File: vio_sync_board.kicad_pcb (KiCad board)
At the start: 2 copper layers, 53 x 64 mm, 3 parts, among them IC1 Pololu 2595, U1 Pololu D24V5F1

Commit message: layout
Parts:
- A1: footprint Module:RaspberryPi_Pico_Common_Unspecified -> Module:RaspberryPi_Pico_Common_THT
- moved A1 42.9 mm to (50.7, 50.2)
- moved IC1 31.5 mm to (86.6, 78.5), turned to -90 degrees
- moved U1 19.5 mm to (81.2, 66.0)
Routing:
- net Net-(IC1-LV): track 42.5 -> 13.2 mm
- net Net-(A1-GPIO13): track 8.64 -> 35.3 mm
- net Net-(A1-3V3): track 57.3 -> 36.6 mm
- net Net-(U1-GND): track 21.3 -> 18.4 mm
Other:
- board outline removed

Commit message: fix traces, add text
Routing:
- net Net-(A1-3V3): track 36.6 -> 48.4 mm
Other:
- board outline added: 45 x 55 mm
- board text added: "VIO SYNC"
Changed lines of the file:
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@@
+		)
+	)
+	(gr_rect
+		(start 46 47.5)
+		(end 91 102.5)
+		(stroke
+			(width 0.05)
+			(type default)
+		)
+		(fill no)
+		(layer "Edge.Cuts")
+	)
+	(gr_text "VIO SYNC"
+		(at 74.5 97 0)
+		(layer "F.SilkS")
+		(effects
+			(font
+				(size 1.5 1.5)
+				(thickness 0.2)
+				(bold yes)
+			)
+			(justify left bottom)
 		)
 	)
@@
 	)
 	(segment
+		(start 86.58 86.12)
+		(end 83.5 83.04)
+		(width 0.2)
+		(layer "B.Cu")
+		(net 12)
+	)
+	(segment
 		(start 74.32 60.4)
 		(end 68.5 60.4)
@@
 	)
 	(segment
-		(start 86.58 86.12)
-		(end 82.824 82.364)
+		(start 75 68.5)
+		(end 78.5 68.5)
+		(width 0.2)
+		(layer "B.Cu")
+		(net 12)
+	)
+	(segment
+		(start 83.5 83)
+		(end 76 83)
+		(width 0.2)
+		(layer "B.Cu")
+		(net 12)
+	)
+	(segment
+		(start 73.5 80.5)
+		(end 73.5 70)
 		(width 0.2)
 		(layer "B.Cu")
@@
 	)
 	(segment
-		(start 82.824 68.904)
+		(start 79.92 67.08)
 		(end 79.92 66)
 		(width 0.2)
@@
 	)
 	(segment
-		(start 82.824 82.364)
-		(end 82.824 68.904)
+		(start 78.5 68.5)
+		(end 79.92 67.08)
 		(width 0.2)
 		(layer "B.Cu")
+		(net 12)
+	)
+	(segment
+		(start 73.5 70)
+		(end 75 68.5)
+		(width 0.2)
+		(layer "B.Cu")
+		(net 12)
+	)
+	(segment
+		(start 76 83)
+		(end 73.5 80.5)
+		(width 0.2)
+		(layer "B.Cu")
+		(net 12)
+	)
+	(segment
+		(start 83.5 83.04)
+		(end 83.5 83)
+		(width 0.2)
+		(layer "B.Cu")

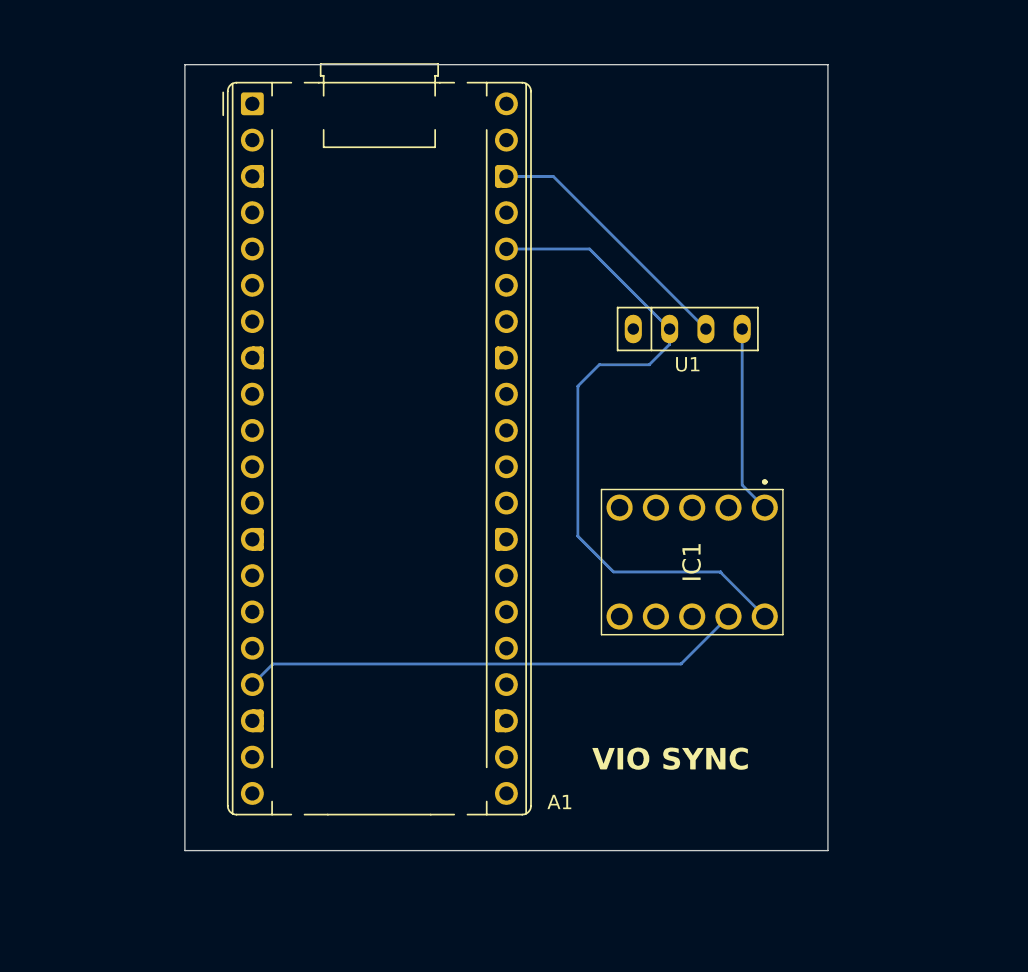
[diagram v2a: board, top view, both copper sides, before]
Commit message: update 1.8v dc convert footprint
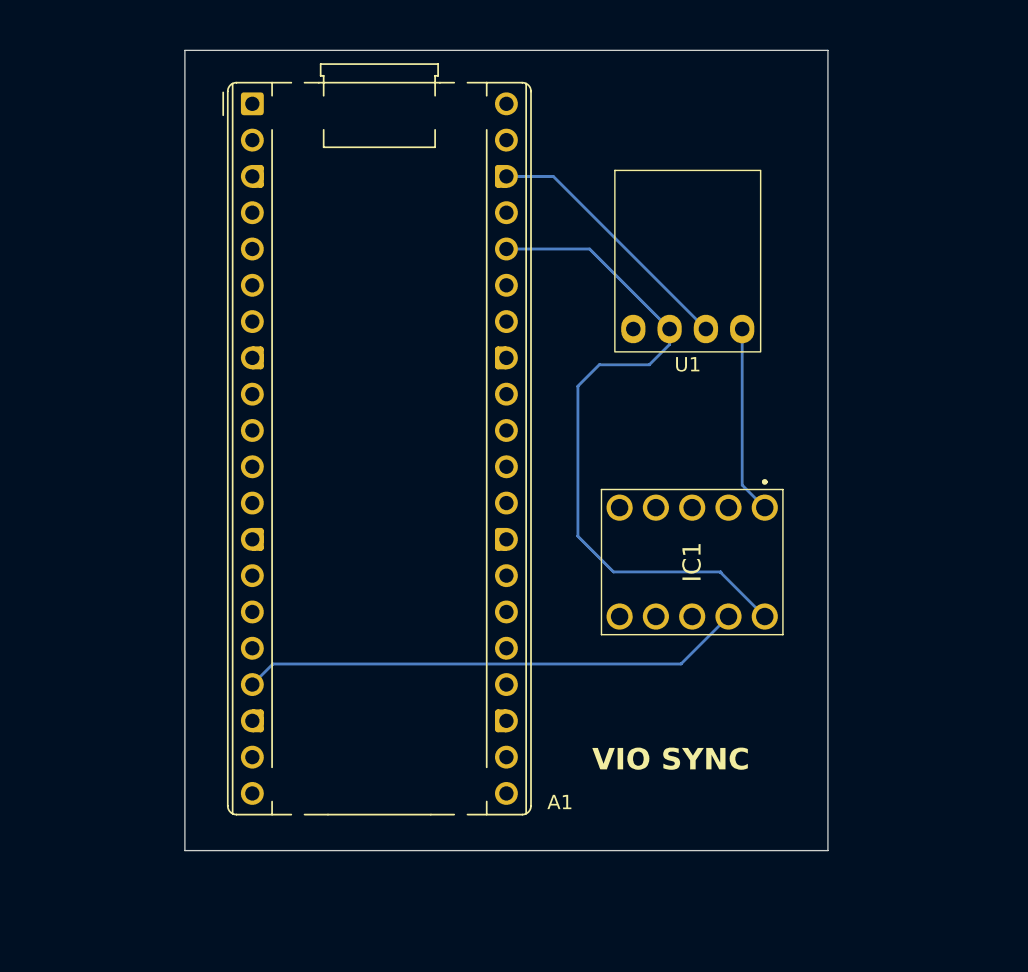
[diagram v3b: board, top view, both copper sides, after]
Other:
- board size 45 x 55 mm -> 45 x 56 mm
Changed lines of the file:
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@@
 		(tenting front back)
 		(pcbplotparams
-			(layerselection 0x00000000_00000000_55555555_5755f5ff)
+			(layerselection 0x00000000_00000000_55555555_575555ff)
 			(plot_on_all_layers_selection 0x00000000_00000000_00000000_00000000)
 			(disableapertmacros no)
@@
 		(sheetfile "vio_sync_board.kicad_sch")
 		(attr through_hole)
-		(fp_line
-			(start -4.91 -1.5)
-			(end 4.91 -1.5)
-			(stroke
-				(width 0.12)
+		(fp_rect
+			(start -5.1 -11.1)
+			(end 5.1 1.6)
+			(stroke
+				(width 0.1)
 				(type default)
 			)
-			(layer "F.SilkS")
-		)
-		(fp_line
-			(start -4.91 1.5)
-			(end -4.91 -1.5)
-			(stroke
-				(width 0.12)
-				(type default)
-			)
-			(layer "F.SilkS")
-		)
-		(fp_line
-			(start -2.54 -1.5)
-			(end -2.54 1.5)
-			(stroke
-				(width 0.12)
-				(type default)
-			)
-			(layer "F.SilkS")
-		)
-		(fp_line
-			(start 4.91 -1.5)
-			(end 4.91 1.5)
-			(stroke
-				(width 0.12)
-				(type default)
-			)
-			(layer "F.SilkS")
-		)
-		(fp_line
-			(start 4.91 1.5)
-			(end -4.91 1.5)
-			(stroke
-				(width 0.12)
-				(type default)
-			)
-			(layer "F.SilkS")
-		)
-		(fp_line
-			(start -4.66 -1.25)
-			(end 4.66 -1.25)
+			(fill no)
+			(layer "F.SilkS")
+		)
+		(fp_rect
+			(start -5.9 -11.9)
+			(end 6.1 2.1)
 			(stroke
 				(width 0.05)
 				(type default)
 			)
-			(layer "F.CrtYd")
-		)
-		(fp_line
-			(start -4.66 1.25)
-			(end -4.66 -1.25)
-			(stroke
-				(width 0.05)
-				(type default)
-			)
-			(layer "F.CrtYd")
-		)
-		(fp_line
-			(start 4.66 -1.25)
-			(end 4.66 1.25)
-			(stroke
-				(width 0.05)
-				(type default)
-			)
-			(layer "F.CrtYd")
-		)
-		(fp_line
-			(start 4.66 1.25)
-			(end -4.66 1.25)
-			(stroke
-				(width 0.05)
-				(type default)
-			)
+			(fill no)
 			(layer "F.CrtYd")
 		)
 		(pad "1" thru_hole oval
 			(at -3.81 0)
-			(size 1.2 2)
-			(drill 0.8)
+			(size 1.7 2)
+			(drill 1.02)
 			(layers "*.Cu" "*.Mask")
 			(remove_unused_layers no)
@@
 		(pad "2" thru_hole oval
 			(at -1.27 0)
-			(size 1.2 2)
-			(drill 0.8)
+			(size 1.7 2)
+			(drill 1.02)
 			(layers "*.Cu" "*.Mask")
 			(remove_unused_layers no)
@@
 		(pad "3" thru_hole oval
 			(at 1.27 0)
-			(size 1.2 2)
-			(drill 0.8)
+			(size 1.7 2)
+			(drill 1.02)
 			(layers "*.Cu" "*.Mask")
 			(remove_unused_layers no)
@@
 		(pad "4" thru_hole oval
 			(at 3.81 0)
-			(size 1.2 2)
-			(drill 0.8)
+			(size 1.7 2)
+			(drill 1.02)
 			(layers "*.Cu" "*.Mask")
 			(remove_unused_layers no)
@@
 	)
 	(gr_rect
-		(start 46 47.5)
+		(start 46 46.5)
 		(end 91 102.5)
 		(stroke

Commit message: start updating layout, not finished
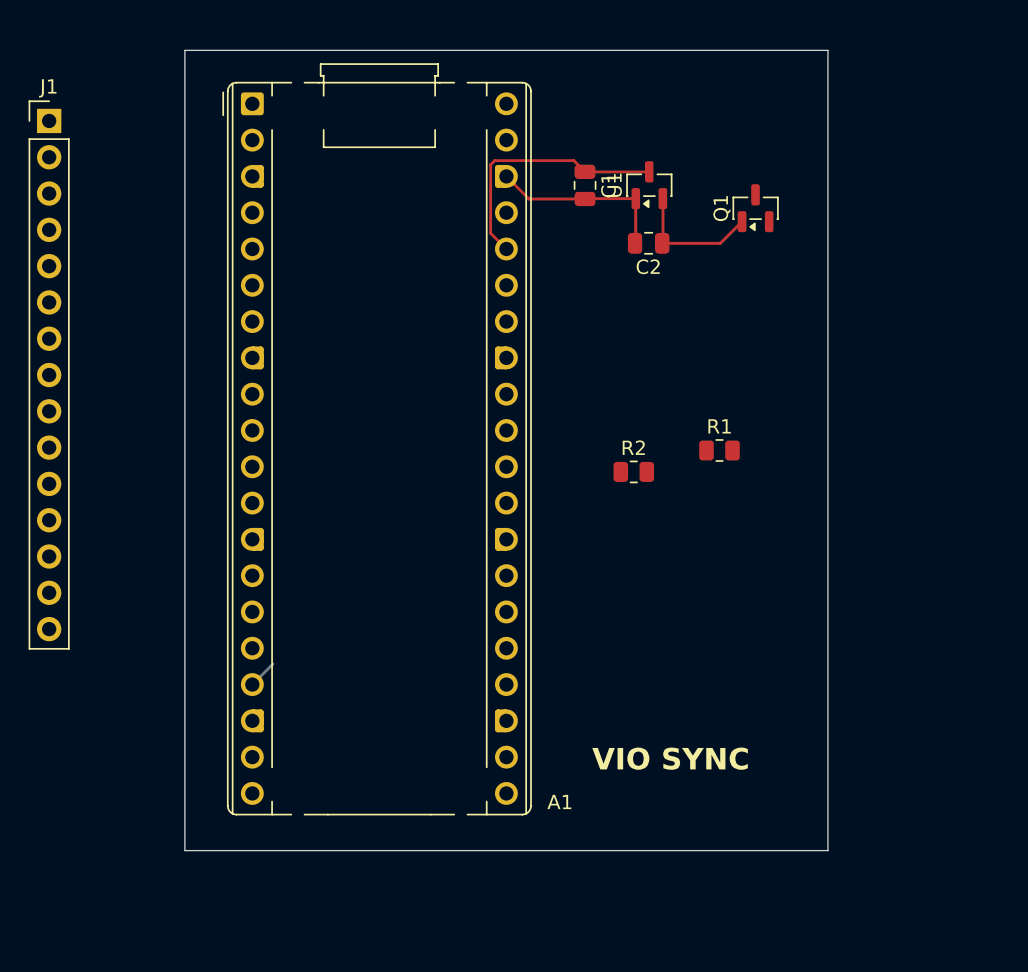
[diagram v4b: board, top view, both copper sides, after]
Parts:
- removed IC1: Pololu 2595, pololu_2595:2595
- added C1: 1uf, Capacitor_SMD:C_0805_2012Metric, F.Cu at (74.0, 56.0)
- added C2: 1uf, Capacitor_SMD:C_0805_2012Metric, F.Cu at (78.5, 60.0)
- added J1: IMU_PI_CAM, Connector_PinHeader_2.54mm:PinHeader_1x15_P2.54mm_Vertical, F.Cu at (36.5, 51.4)
- added Q1: BSS138, Package_TO_SOT_SMD:SOT-23, F.Cu at (85.9, 57.5)
- added R1: 10k, Resistor_SMD:R_0805_2012Metric, F.Cu at (83.4, 74.5)
- added R2: 10k, Resistor_SMD:R_0805_2012Metric, F.Cu at (77.4, 76.0)
- U1: value Pololu D24V5F1 -> MCP1700x-180xxTT; footprint pololu_2840:D24V5F1 -> Package_TO_SOT_SMD:SOT-23
- moved U1 10.4 mm to (78.5, 55.9), turned to 90 degrees
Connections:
- A1 pad 1: unconnected-(A1-GPIO0-Pad1) -> /UART0_TX
- A1 pad 13: Net-(U1-GND) -> /GND
- A1 pad 17: Net-(A1-GPIO13) -> /XTR_3V3
- A1 pad 18: Net-(U1-GND) -> /GND
- A1 pad 19: unconnected-(A1-GPIO14-Pad19) -> /TSYNC
- A1 pad 2: unconnected-(A1-GPIO1-Pad2) -> /UART0_RX
- A1 pad 20: unconnected-(A1-GPIO15-Pad20) -> /INT
- A1 pad 21: unconnected-(A1-GPIO16-Pad21) -> /POCI
- A1 pad 22: unconnected-(A1-GPIO17-Pad22) -> /CS
- A1 pad 23: Net-(U1-GND) -> /GND
- A1 pad 24: unconnected-(A1-GPIO18-Pad24) -> /SPI0_SCK
- A1 pad 25: unconnected-(A1-GPIO19-Pad25) -> /PICO
- A1 pad 28: Net-(U1-GND) -> /GND
- A1 pad 3: Net-(U1-GND) -> /GND
- A1 pad 36: Net-(A1-3V3) -> /3V3
- A1 pad 38: Net-(U1-GND) -> /GND
- A1 pad 39: unconnected-(A1-VSYS-Pad39) -> /VSYS
- A1 pad 8: Net-(U1-GND) -> /GND
- U1 pad 1: unconnected-(U1-SHDN-Pad1) -> /GND
- U1 pad 2: Net-(A1-3V3) -> Net-(Q1-G)
- U1 pad 3: Net-(U1-GND) -> /3V3
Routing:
- net Net-(A1-3V3): track 48.4 -> 0.00 mm
- net Net-(A1-GPIO13): track 35.3 -> 0.00 mm
- net Net-(U1-GND): track 18.4 -> 0.00 mm
- net /3V3: track 0.00 -> 17.9 mm
- net Net-(IC1-LV): track 13.2 -> 0.00 mm
- net /GND: track 0.00 -> 12.9 mm
- net Net-(Q1-G): track 0.00 -> 9.36 mm
- net /XTR_3V3: track 0.00 -> 2.04 mm

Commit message: maybe we should split header to 3?
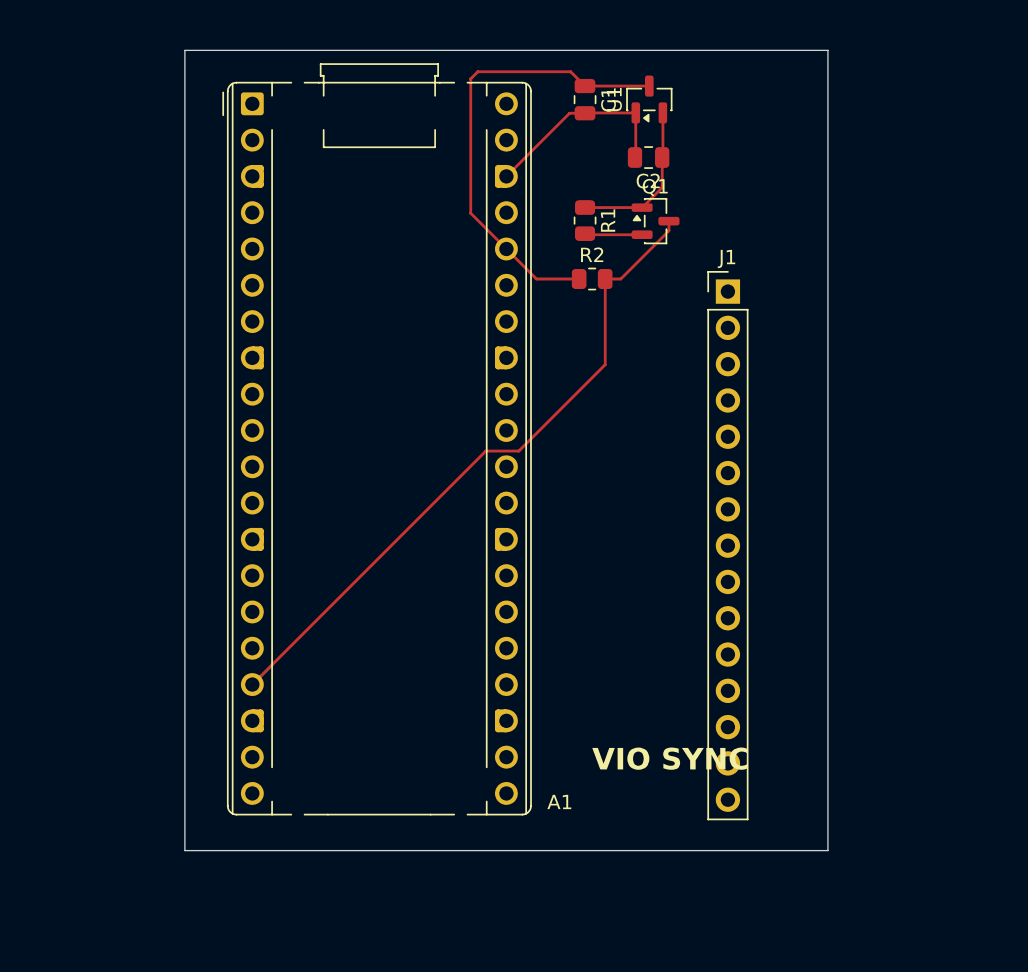
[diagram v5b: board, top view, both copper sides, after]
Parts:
- moved J1 49.0 mm to (84.0, 63.4)
- moved R1 18.6 mm to (74.0, 58.4), turned to -90 degrees
- moved R2 13.8 mm to (74.5, 62.5)
- moved Q1 7.06 mm to (78.9, 58.5), turned to 0 degrees
- moved C1 6.00 mm to (74.0, 50.0)
- moved C2 6.00 mm to (78.5, 54.0)
- moved U1 6.00 mm to (78.5, 49.9)
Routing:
- net /XTR_3V3: track 2.04 -> 48.5 mm
- net /3V3: track 17.9 -> 32.0 mm
- net /XTR_1V8: track 0.00 -> 4.03 mm
- net Net-(Q1-G): track 9.36 -> 11.2 mm
- net /GND: track 12.9 -> 14.0 mm

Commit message: refine pin header
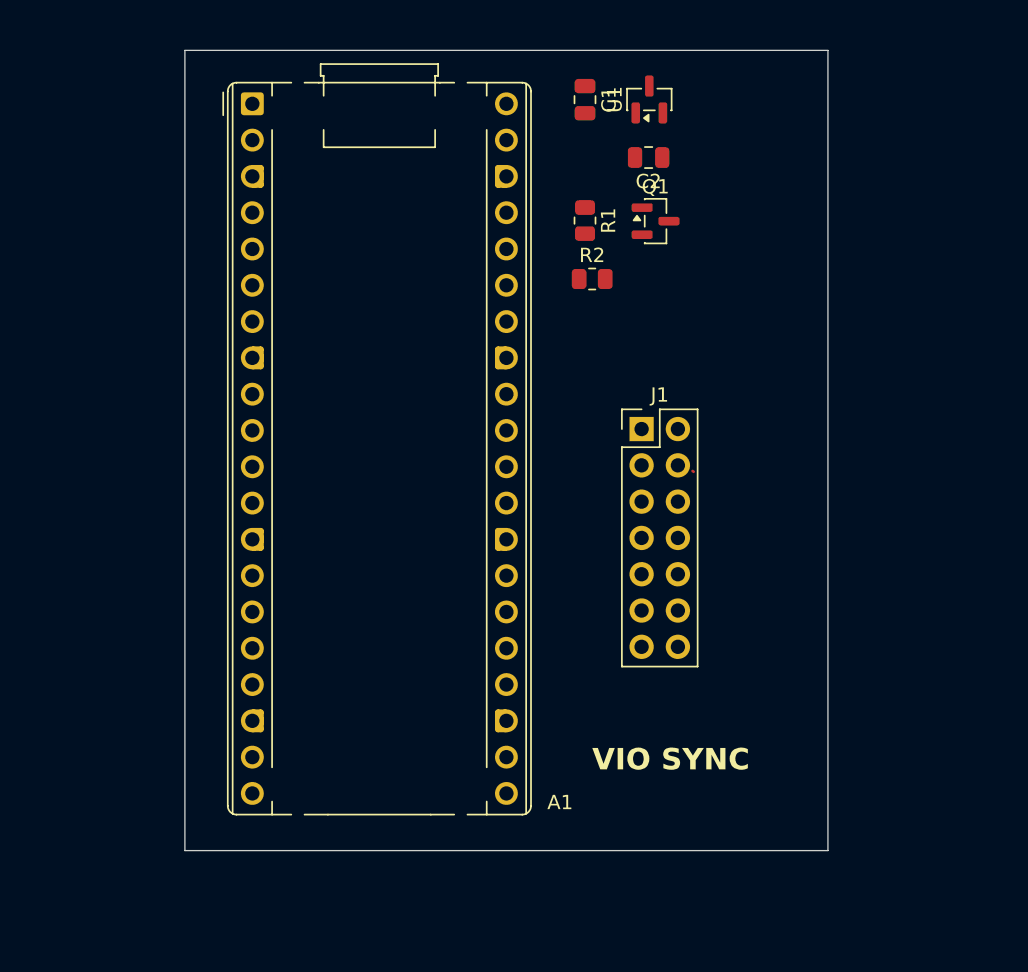
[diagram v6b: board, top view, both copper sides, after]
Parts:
- J1: value IMU_PI_CAM -> Conn_Pi_Imu_Cam; footprint Connector_PinHeader_2.54mm:PinHeader_1x15_P2.54mm_Vertical -> Connector_PinHeader_2.54mm:PinHeader_2x07_P2.54mm_Vertical
- moved J1 11.4 mm to (78.0, 73.0)
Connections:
- net /CS renamed /SPI0_CS
- net /INT renamed /IMU_INT
- net /PICO renamed /SPI0_PICO
- net /POCI renamed /SPI0_POCI
- J1 pad 10: /GND -> /VSYS
- J1 pad 12: /XTR_1V8 -> /UART0_RX
- J1 pad 13: /GND -> /UART0_TX
- J1 pad 14: /VSYS -> /GND
- J1 pad 8: /UART0_TX -> /GND
- J1 pad 9: /UART0_RX -> /XTR_1V8
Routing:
- net /XTR_3V3: track 48.5 -> 0.00 mm
- net /3V3: track 32.0 -> 0.00 mm
- net /GND: track 14.0 -> 0.07 mm
- net Net-(Q1-G): track 11.2 -> 0.00 mm
- net /XTR_1V8: track 4.03 -> 0.10 mm

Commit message: layout
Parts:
- J1: value Conn_Pi_Imu_Cam -> Conn_IMU_Pi_Cam
- moved Q1 1.86 mm to (80.4, 59.5)
- moved J1 1.34 mm to (78.5, 71.8)
- moved C2 1.05 mm to (79.5, 54.0)
- moved U1 1.00 mm to (79.5, 49.9)
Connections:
- J1 pad 1: /GND -> /3V3
- J1 pad 11: /TSYNC -> /SPI0_POCI
- J1 pad 12: /UART0_RX -> /XTR_1V8
- J1 pad 13: /UART0_TX -> /IMU_INT
- J1 pad 2: /IMU_INT -> /GND
- J1 pad 3: /SPI0_POCI -> /SPI0_PICO
- J1 pad 4: /SPI0_CS -> /UART0_TX
- J1 pad 6: /SPI0_PICO -> /UART0_RX
- J1 pad 7: /3V3 -> /GND
- J1 pad 8: /GND -> /TSYNC
- J1 pad 9: /XTR_1V8 -> /SPI0_CS
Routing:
- net /GND: track 0.07 -> 58.3 mm
- net /UART0_RX: track 0.00 -> 57.1 mm
- net /XTR_3V3: track 0.00 -> 49.6 mm
- net /3V3: track 0.00 -> 47.5 mm
- net /TSYNC: track 0.00 -> 43.7 mm
- net /UART0_TX: track 0.00 -> 43.6 mm
- net /IMU_INT: track 0.00 -> 40.6 mm
- net /VSYS: track 0.00 -> 36.8 mm
- net /XTR_1V8: track 0.10 -> 36.3 mm
- net /SPI0_POCI: track 0.00 -> 20.5 mm
- net /SPI0_PICO: track 0.00 -> 18.7 mm
- net /SPI0_SCK: track 0.00 -> 18.3 mm
- net /SPI0_CS: track 0.00 -> 18.2 mm
- net Net-(Q1-G): track 0.00 -> 14.1 mm
